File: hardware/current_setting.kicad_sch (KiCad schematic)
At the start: 10 parts, among them U2 ADTL084

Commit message: Updates to structure of the schematic. Minor funcitonality adjustments.
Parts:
- removed R23, R24, R28: R_Small, symbol Device:R_Small
- removed R29, R30: 0, symbol Device:R_Small
- removed RV3: R_Potentiometer_Small, symbol Device:R_Potentiometer_Small
- added R31, R32, R34: 0R, Resistor_SMD:R_0805_2012Metric_Pad1.20x1.40mm_HandSolder, symbol Device:R_Small
- added R36, R40: R_Small, Resistor_SMD:R_0805_2012Metric_Pad1.20x1.40mm_HandSolder, symbol Device:R_Small
- R33: renamed from R27; value R_Small -> 0R; footprint (none) -> Resistor_SMD:R_0805_2012Metric_Pad1.20x1.40mm_HandSolder
- R35: renamed from R25; footprint (none) -> Resistor_SMD:R_0805_2012Metric_Pad1.20x1.40mm_HandSolder
- R39: renamed from R26; footprint (none) -> Resistor_SMD:R_0805_2012Metric_Pad1.20x1.40mm_HandSolder
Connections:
- net curr_set_A_uC is gone; now on net GND: R33.2
- net GND: now also R34.2, R36.2, R40.2
- net at R33.1, U2.12 (+): now also R31.2
- net at U2.10 (+): now also R32.2, R34.1
- net at R35.2, U2.13 (-): now also R36.1
- net at R39.2, U2.9 (-): now also R40.1
- net set_curr_A renamed opStage1A_ang_g
- net set_curr_B renamed opStage1B_ang_g
- new net dacOutA_ang_g: R31.1
- new net dacOutB_ang_g: R32.1
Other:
- moved on the sheet: R35, R39, U2C, U2D

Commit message: Began initial routing. Schematic still not fully complete.
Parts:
- renumbered R31 to R500, R33 to R501, R35 to R502, R36 to R503, R32 to R504, R34 to R505, R39 to R506, R40 to R507
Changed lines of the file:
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@@
   (symbol (lib_id "power:GND") (at 72.39 122.555 0) (unit 1)
     (in_bom yes) (on_board yes) (dnp no) (fields_autoplaced)
-    (property "Reference" "#PWR034" (at 72.39 128.905 0)
+    (property "Reference" "#PWR0502" (at 72.39 128.905 0)
       (effects (font (size 1.27 1.27)) hide)
     )
@@
       (project "current_sink_dev"
         (path "/695b42ec-77e0-4be3-bf4d-1fc5cfcb9ef1/c8c24e40-4b1c-44b1-836c-5d981daf7982"
-          (reference "#PWR034") (unit 1)
+          (reference "#PWR0502") (unit 1)
         )
       )
@@
   (symbol (lib_id "Device:R_Small") (at 72.39 50.8 0) (unit 1)
     (in_bom yes) (on_board yes) (dnp no) (fields_autoplaced)
-    (property "Reference" "R33" (at 74.93 50.165 0)
+    (property "Reference" "R501" (at 74.93 50.165 0)
       (effects (font (size 1.27 1.27)) (justify left))
     )
@@
       (project "current_sink_dev"
         (path "/695b42ec-77e0-4be3-bf4d-1fc5cfcb9ef1/c8c24e40-4b1c-44b1-836c-5d981daf7982"
-          (reference "R33") (unit 1)
+          (reference "R501") (unit 1)
         )
       )
@@
   (symbol (lib_id "Device:R_Small") (at 72.39 38.1 0) (unit 1)
     (in_bom yes) (on_board yes) (dnp no) (fields_autoplaced)
-    (property "Reference" "R31" (at 74.93 37.465 0)
+    (property "Reference" "R500" (at 74.93 37.465 0)
       (effects (font (size 1.27 1.27)) (justify left))
     )
@@
       (project "current_sink_dev"
         (path "/695b42ec-77e0-4be3-bf4d-1fc5cfcb9ef1/c8c24e40-4b1c-44b1-836c-5d981daf7982"
-          (reference "R31") (unit 1)
+          (reference "R500") (unit 1)
         )
       )
@@
   (symbol (lib_id "Device:R_Small") (at 72.39 97.79 0) (unit 1)
     (in_bom yes) (on_board yes) (dnp no) (fields_autoplaced)
-    (property "Reference" "R32" (at 74.93 97.155 0)
+    (property "Reference" "R504" (at 74.93 97.155 0)
       (effects (font (size 1.27 1.27)) (justify left))
     )
@@
       (project "current_sink_dev"
         (path "/695b42ec-77e0-4be3-bf4d-1fc5cfcb9ef1/c8c24e40-4b1c-44b1-836c-5d981daf7982"
-          (reference "R32") (unit 1)
-        )
-      )
-    )
-  )
-  (symbol (lib_id "User_Opamp:ADTL084") (at 118.11 46.99 0) (unit 4)
-    (in_bom yes) (on_board yes) (dnp no) (fields_autoplaced)
-    (property "Reference" "U2" (at 118.11 38.1 0)
-      (effects (font (size 1.27 1.27)))
-    )
-    (property "Value" "ADTL084" (at 118.11 40.64 0)
-      (effects (font (size 1.27 1.27)))
+          (reference "R504") (unit 1)
+        )
+      )
+    )
+  )
+  (symbol (lib_name "ADTL084_1") (lib_id "User_Opamp:ADTL084") (at 118.11 46.99 0) (unit 4)
+    (in_bom yes) (on_board yes) (dnp no)
+    (property "Reference" "U2" (at 118.11 39.37 0)
+      (effects (font (size 1.27 1.27)) (justify left))
+    )
+    (property "Value" "ADTL084" (at 118.11 41.91 0)
+      (effects (font (size 1.27 1.27)) (justify left))
     )
     (property "Footprint" "Package_SO:SOIC-14_3.9x8.7mm_P1.27mm" (at 121.285 40.005 0)
@@
     )
     (pin "1")
-    (pin "13")
-    (pin "16")
     (pin "2")
     (pin "3")
@@
     (pin "14")
     (pin "11")
-    (pin "17")
     (pin "4")
     (instances
@@
         )
         (path "/695b42ec-77e0-4be3-bf4d-1fc5cfcb9ef1/02da786d-4b46-4498-8c46-331dfb2a8a58"
-          (reference "U2") (unit 4)
-        )
-        (path "/695b42ec-77e0-4be3-bf4d-1fc5cfcb9ef1/c8c24e40-4b1c-44b1-836c-5d981daf7982"
-          (reference "U2") (unit 4)
+          (reference "U201") (unit 4)
+        )
+        (path "/695b42ec-77e0-4be3-bf4d-1fc5cfcb9ef1/c8c24e40-4b1c-44b1-836c-5d981daf7982"
+          (reference "U201") (unit 4)
         )
       )
@@
   (symbol (lib_id "power:GND") (at 104.14 72.39 0) (unit 1)
     (in_bom yes) (on_board yes) (dnp no) (fields_autoplaced)
-    (property "Reference" "#PWR017" (at 104.14 78.74 0)
+    (property "Reference" "#PWR0501" (at 104.14 78.74 0)
       (effects (font (size 1.27 1.27)) hide)
     )
@@
       (project "current_sink_dev"
         (path "/695b42ec-77e0-4be3-bf4d-1fc5cfcb9ef1/c8c24e40-4b1c-44b1-836c-5d981daf7982"
-          (reference "#PWR017") (unit 1)
+          (reference "#PWR0501") (unit 1)
         )
       )
@@
   (symbol (lib_id "Device:R_Small") (at 118.11 118.11 270) (unit 1)
     (in_bom yes) (on_board yes) (dnp no) (fields_autoplaced)
-    (property "Reference" "R39" (at 118.11 113.03 90)
+    (property "Reference" "R506" (at 118.11 113.03 90)
       (effects (font (size 1.27 1.27)))
     )
@@
       (project "current_sink_dev"
         (path "/695b42ec-77e0-4be3-bf4d-1fc5cfcb9ef1/c8c24e40-4b1c-44b1-836c-5d981daf7982"
-          (reference "R39") (unit 1)
+          (reference "R506") (unit 1)
         )
       )
@@
   (symbol (lib_id "Device:R_Small") (at 104.14 64.77 0) (unit 1)
     (in_bom yes) (on_board yes) (dnp no) (fields_autoplaced)
-    (property "Reference" "R36" (at 106.605 64.135 0)
+    (property "Reference" "R503" (at 106.605 64.135 0)
       (effects (font (size 1.27 1.27)) (justify left))
     )
@@
       (project "current_sink_dev"
         (path "/695b42ec-77e0-4be3-bf4d-1fc5cfcb9ef1/c8c24e40-4b1c-44b1-836c-5d981daf7982"
-          (reference "R36") (unit 1)
+          (reference "R503") (unit 1)
         )
       )
@@
     )
     (pin "1")
-    (pin "13")
-    (pin "16")
     (pin "2")
     (pin "3")
@@
     (pin "14")
     (pin "11")
-    (pin "17")
     (pin "4")
     (instances
@@
         )
         (path "/695b42ec-77e0-4be3-bf4d-1fc5cfcb9ef1/c8c24e40-4b1c-44b1-836c-5d981daf7982"
-          (reference "U4") (unit 4)
+          (reference "U202") (unit 4)
         )
       )
@@
   (symbol (lib_id "power:GND") (at 72.39 62.865 0) (unit 1)
     (in_bom yes) (on_board yes) (dnp no) (fields_autoplaced)
-    (property "Reference" "#PWR016" (at 72.39 69.215 0)
+    (property "Reference" "#PWR0500" (at 72.39 69.215 0)
       (effects (font (size 1.27 1.27)) hide)
     )
@@
       (project "current_sink_dev"
         (path "/695b42ec-77e0-4be3-bf4d-1fc5cfcb9ef1/c8c24e40-4b1c-44b1-836c-5d981daf7982"
-          (reference "#PWR016") (unit 1)
+          (reference "#PWR0500") (unit 1)
         )
       )
@@
   (symbol (lib_id "Device:R_Small") (at 104.14 124.46 0) (unit 1)
     (in_bom yes) (on_board yes) (dnp no) (fields_autoplaced)
-    (property "Reference" "R40" (at 106.605 123.825 0)
+    (property "Reference" "R507" (at 106.605 123.825 0)
       (effects (font (size 1.27 1.27)) (justify left))
     )
@@
       (project "current_sink_dev"
         (path "/695b42ec-77e0-4be3-bf4d-1fc5cfcb9ef1/c8c24e40-4b1c-44b1-836c-5d981daf7982"
-          (reference "R40") (unit 1)
+          (reference "R507") (unit 1)
         )
       )
@@
   (symbol (lib_id "Device:R_Small") (at 118.11 58.42 270) (unit 1)
     (in_bom yes) (on_board yes) (dnp no) (fields_autoplaced)
-    (property "Reference" "R35" (at 118.11 53.34 90)
+    (property "Reference" "R502" (at 118.11 53.34 90)
       (effects (font (size 1.27 1.27)))
     )
@@
       (project "current_sink_dev"
         (path "/695b42ec-77e0-4be3-bf4d-1fc5cfcb9ef1/c8c24e40-4b1c-44b1-836c-5d981daf7982"
-          (reference "R35") (unit 1)
+          (reference "R502") (unit 1)
         )
       )
@@
   (symbol (lib_id "Device:R_Small") (at 72.39 110.49 0) (unit 1)
     (in_bom yes) (on_board yes) (dnp no) (fields_autoplaced)
-    (property "Reference" "R34" (at 74.93 109.855 0)
+    (property "Reference" "R505" (at 74.93 109.855 0)
       (effects (font (size 1.27 1.27)) (justify left))
     )
@@
       (project "current_sink_dev"
         (path "/695b42ec-77e0-4be3-bf4d-1fc5cfcb9ef1/c8c24e40-4b1c-44b1-836c-5d981daf7982"
-          (reference "R34") (unit 1)
+          (reference "R505") (unit 1)
         )
       )
@@
   (symbol (lib_id "power:GND") (at 104.14 132.08 0) (unit 1)
     (in_bom yes) (on_board yes) (dnp no) (fields_autoplaced)
-    (property "Reference" "#PWR018" (at 104.14 138.43 0)
+    (property "Reference" "#PWR0503" (at 104.14 138.43 0)
       (effects (font (size 1.27 1.27)) hide)
     )
@@
       (project "current_sink_dev"
         (path "/695b42ec-77e0-4be3-bf4d-1fc5cfcb9ef1/c8c24e40-4b1c-44b1-836c-5d981daf7982"
-          (reference "#PWR018") (unit 1)
-        )
-      )
+          (reference "#PWR0503") (unit 1)
+        )
+      )

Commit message: Routing close to completion. Pending review.
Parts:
- added TP500 (x2): ~, TestPoint:TestPoint_Pad_D1.0mm, symbol Connector:TestPoint
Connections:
- net at R500.2, R501.1, U2.12 (+): now also TP500.1
- net at R504.2, R505.1, U2.10 (+): now also TP500.1
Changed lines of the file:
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@@
   (junction (at 129.54 46.99) (diameter 0) (color 0 0 0 0)
   )
+  (junction (at 87.63 44.45) (diameter 0) (color 0 0 0 0)
+  )
   (junction (at 72.39 44.45) (diameter 0) (color 0 0 0 0)
   )
@@
   (junction (at 72.39 104.14) (diameter 0) (color 0 0 0 0)
   )
+  (junction (at 87.63 104.14) (diameter 0) (color 0 0 0 0)
+  )
   (junction (at 104.14 58.42) (diameter 0) (color 0 0 0 0)
   )
@@
     (stroke (width 0) (type default))
   )
+  (wire (pts (xy 87.63 104.14) (xy 110.49 104.14))
+    (stroke (width 0) (type default))
+  )
   (wire (pts (xy 104.14 58.42) (xy 104.14 62.23))
     (stroke (width 0) (type default))
   )
-  (wire (pts (xy 72.39 44.45) (xy 110.49 44.45))
+  (wire (pts (xy 72.39 44.45) (xy 87.63 44.45))
     (stroke (width 0) (type default))
   )
@@
     (stroke (width 0) (type default))
   )
+  (wire (pts (xy 87.63 44.45) (xy 110.49 44.45))
+    (stroke (width 0) (type default))
+  )
   (wire (pts (xy 129.54 106.68) (xy 147.32 106.68))
     (stroke (width 0) (type default))
@@
     (stroke (width 0) (type default))
   )
-  (wire (pts (xy 72.39 104.14) (xy 110.49 104.14))
+  (wire (pts (xy 72.39 104.14) (xy 87.63 104.14))
     (stroke (width 0) (type default))
   )
@@
     (property "Intersheetrefs" "${INTERSHEET_REFS}" (at 166.8563 106.68 0)
       (effects (font (size 1.27 1.27)) (justify left) hide)
+    )
+  )
+  (symbol (lib_id "Connector:TestPoint") (at 87.63 44.45 0) (unit 1)
+    (in_bom yes) (on_board yes) (dnp no) (fields_autoplaced)
+    (property "Reference" "TP500" (at 89.535 41.783 0)
+      (effects (font (size 1.27 1.27)) (justify left))
+    )
+    (property "Value" "~" (at 89.535 43.053 0)
+      (effects (font (size 1.27 1.27)) (justify left))
+    )
+    (property "Footprint" "TestPoint:TestPoint_Pad_D1.0mm" (at 92.71 44.45 0)
+      (effects (font (size 1.27 1.27)) hide)
+    )
+    (property "Datasheet" "~" (at 92.71 44.45 0)
+      (effects (font (size 1.27 1.27)) hide)
+    )
+    (pin "1")
+    (instances
+      (project "current_sink_dev"
+        (path "/695b42ec-77e0-4be3-bf4d-1fc5cfcb9ef1/02451f10-14c4-4640-81bd-2617f523efcf"
+          (reference "TP500") (unit 1)
+        )
+        (path "/695b42ec-77e0-4be3-bf4d-1fc5cfcb9ef1/0c6362b3-70d1-4005-b89b-9ee91ccddbc7"
+          (reference "TP514") (unit 1)
+        )
+        (path "/695b42ec-77e0-4be3-bf4d-1fc5cfcb9ef1/c8c24e40-4b1c-44b1-836c-5d981daf7982"
+          (reference "TP518") (unit 1)
+        )
+      )
     )
   )
@@
         )
       )
+    )
+  )
+  (symbol (lib_id "Connector:TestPoint") (at 87.63 104.14 0) (unit 1)
+    (in_bom yes) (on_board yes) (dnp no) (fields_autoplaced)
+    (property "Reference" "TP500" (at 89.535 101.473 0)
+      (effects (font (size 1.27 1.27)) (justify left))
+    )
+    (property "Value" "~" (at 89.535 102.743 0)
+      (effects (font (size 1.27 1.27)) (justify left))
+    )
+    (property "Footprint" "TestPoint:TestPoint_Pad_D1.0mm" (at 92.71 104.14 0)
+      (effects (font (size 1.27 1.27)) hide)
+    )
+    (property "Datasheet" "~" (at 92.71 104.14 0)
+      (effects (font (size 1.27 1.27)) hide)
+    )
+    (pin "1")
+    (instances
+      (project "current_sink_dev"
+        (path "/695b42ec-77e0-4be3-bf4d-1fc5cfcb9ef1/02451f10-14c4-4640-81bd-2617f523efcf"
+          (reference "TP500") (unit 1)
+        )
+        (path "/695b42ec-77e0-4be3-bf4d-1fc5cfcb9ef1/0c6362b3-70d1-4005-b89b-9ee91ccddbc7"
+          (reference "TP513") (unit 1)
+        )
+        (path "/695b42ec-77e0-4be3-bf4d-1fc5cfcb9ef1/c8c24e40-4b1c-44b1-836c-5d981daf7982"
+          (reference "TP517") (unit 1)
+        )
+      )

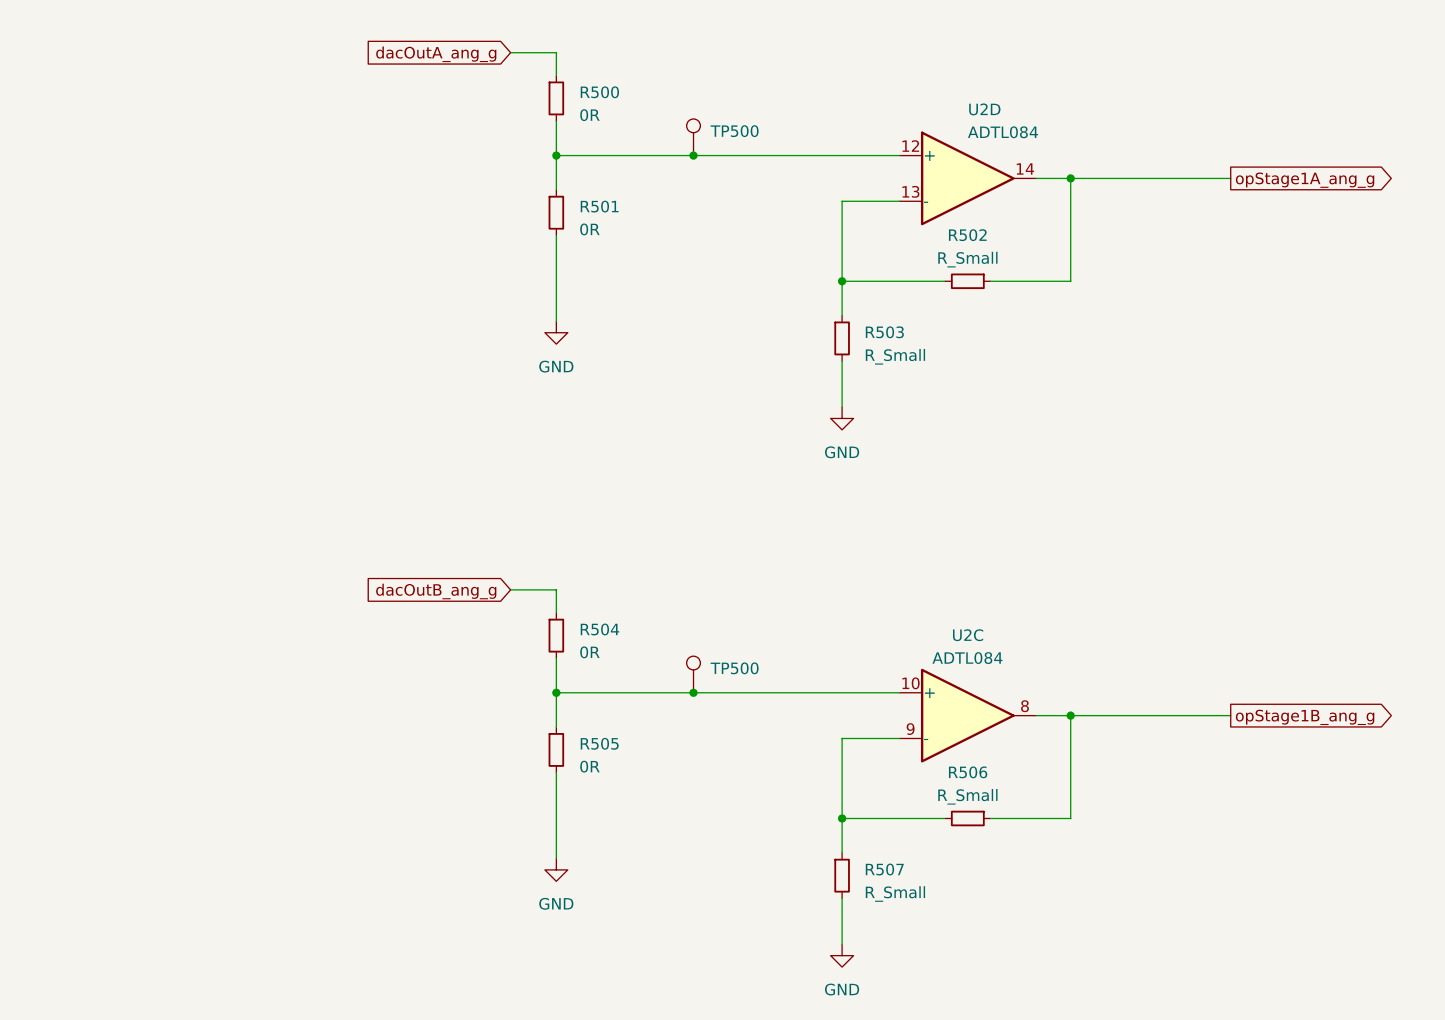
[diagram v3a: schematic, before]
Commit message: Added some doucmentation to MCP driver
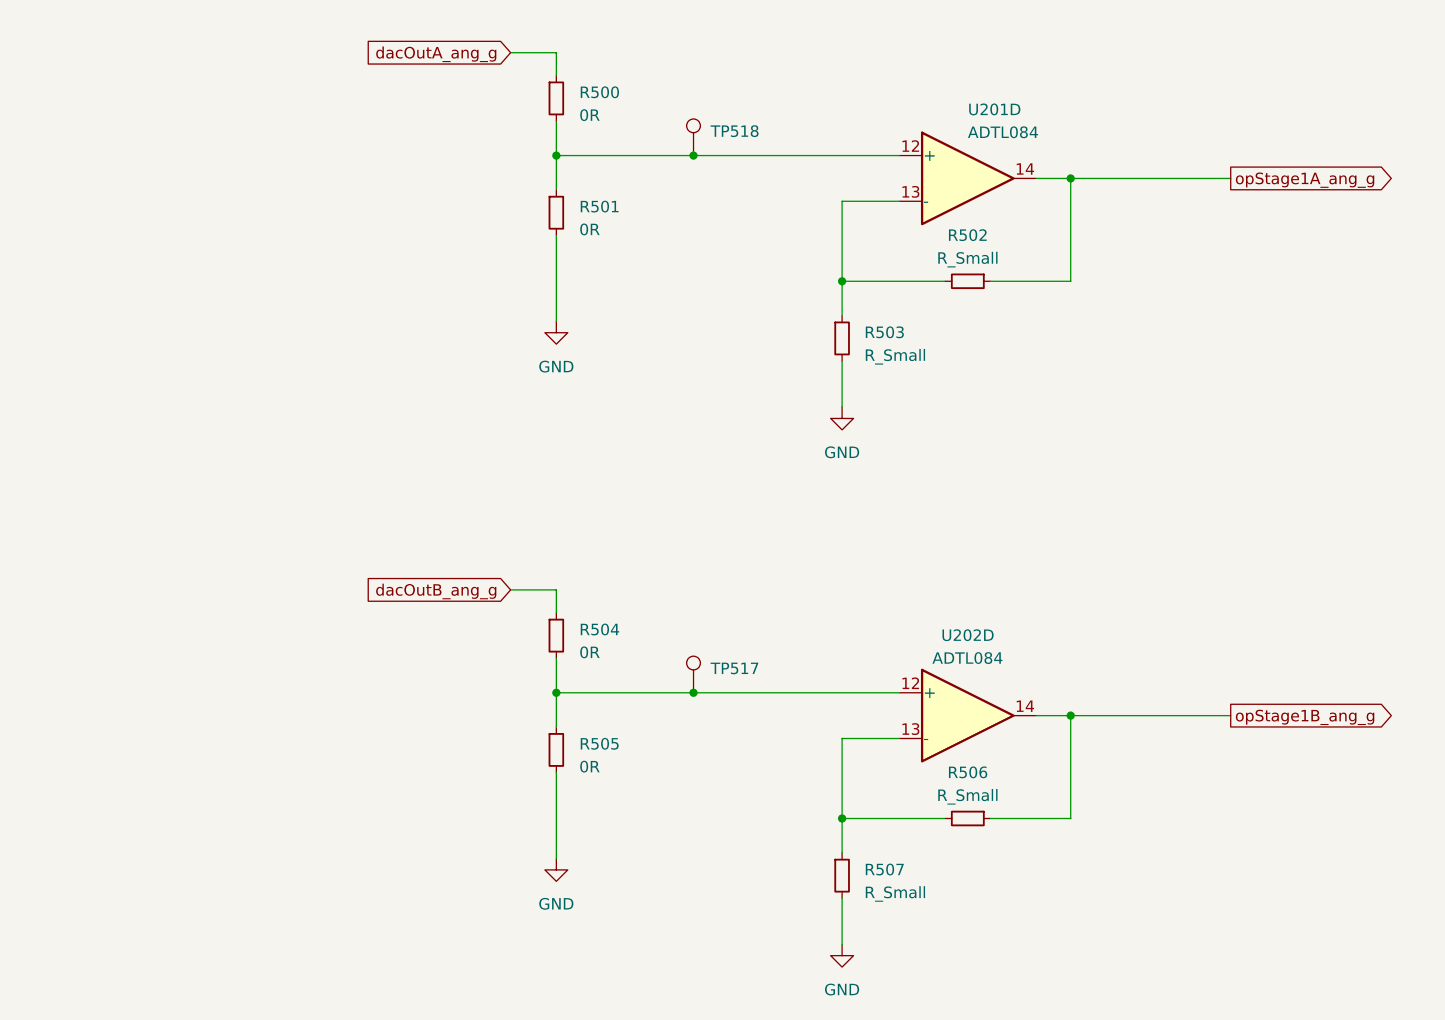
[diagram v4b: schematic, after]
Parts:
- renumbered TP500 to TP517, TP500 to TP518, U2 to U201, U2 to U202
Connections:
- net opStage1B_ang_g: now also U202.14; no longer U202.8
- net at R504.2, R505.1, TP517.1: now also U202.12 (+); no longer U202.10 (+)
- net at R506.2, R507.1: now also U202.13 (-); no longer U202.9 (-)
